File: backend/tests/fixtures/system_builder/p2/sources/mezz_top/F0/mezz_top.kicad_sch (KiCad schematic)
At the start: 2 parts, among them J1 DF12_Receptacle_2x10, J2 DF12_Receptacle_2x10

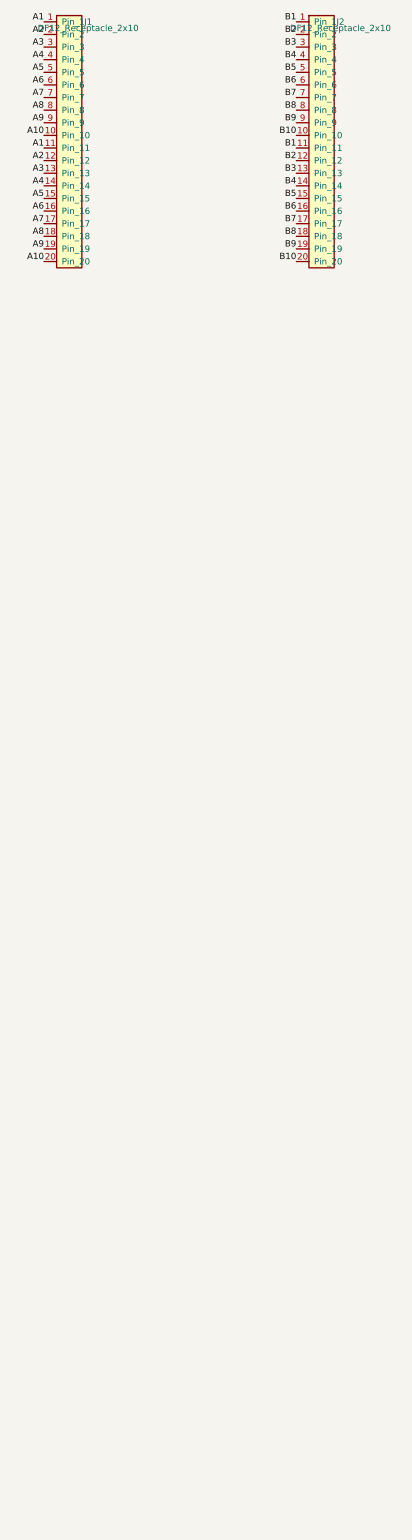
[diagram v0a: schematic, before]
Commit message: SB2-21: rebuild the mezzanine fixtures on Samtec ADM6/ADF6
The SB2-21 review moved the mezzanine pair from Hirose DF12(3.0) to Samtec
ADM6-30-03.5-L-4-0-A / ADF6-30-03.5-L-4-0-A, the JTYU OBC-to-CMBD pair.

- Footprints are written from Samtec's recommended PCB layouts (ADM6 rev G,
  ADF6 rev H): 4x30 at 0.635 mm, 0.356 mm pads, -A alignment NPTHs. They
  match Pixxel's ADM6-30 library footprint and CMBD's ADF6-30 pad for pad.
- Goldens: mated height 7.00 mm (ADX6 mated views, Table 1), top pose
  (0, 0, 8.6) mm, body heights G 4.900 / K 3.230 mm. The footprints name no
  orientation, so frames infer at medium confidence; goldens now pin the
  confidence of every frame.
- Samtec's STEP files (git-ignored, from the JTYU repos) are placed with
  rotate (-90 0 0); their alignment pins land on the NPTHs in KiCad's GLB
  export, which fixes the pin-1 end.
- All six boards clean on ERC, DRC with schematic parity, netlist, STEP and
  GLB with KiCad 10.0.6.
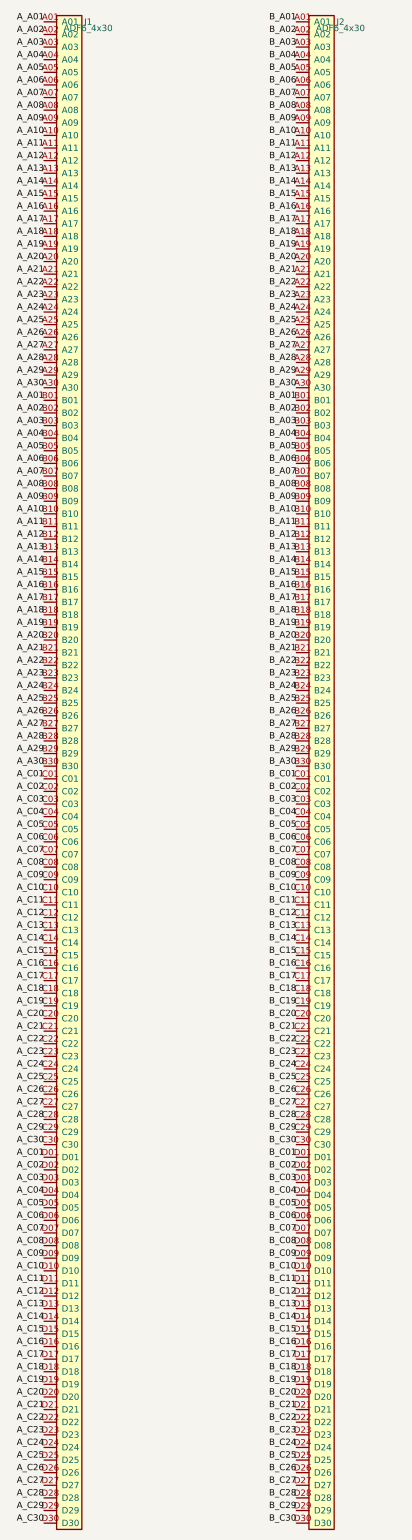
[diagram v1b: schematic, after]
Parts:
- J1, J2: value DF12_Receptacle_2x10 -> ADF6_4x30; footprint PrismFixture:Hirose_DF12_DF12C3.0-20DS-0.5V_2x10_P0.50mm_Vertical -> PrismFixture:Samtec_ADF6-30-03.5-L-4-0-A; symbol PrismFixture:DF12_Receptacle_2x10 -> PrismFixture:ADF6_4x30
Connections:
- removed net A1: J1.1 (Pin_1), J1.11 (Pin_11)
- removed net A10: J1.10 (Pin_10), J1.20 (Pin_20)
- removed net A2: J1.12 (Pin_12), J1.2 (Pin_2)
- removed net A3: J1.13 (Pin_13), J1.3 (Pin_3)
- removed net A4: J1.14 (Pin_14), J1.4 (Pin_4)
- removed net A5: J1.15 (Pin_15), J1.5 (Pin_5)
- removed net A6: J1.16 (Pin_16), J1.6 (Pin_6)
- removed net A7: J1.17 (Pin_17), J1.7 (Pin_7)
- removed net A8: J1.18 (Pin_18), J1.8 (Pin_8)
- removed net A9: J1.19 (Pin_19), J1.9 (Pin_9)
- removed net B1: J2.1 (Pin_1), J2.11 (Pin_11)
- removed net B10: J2.10 (Pin_10), J2.20 (Pin_20)
- removed net B2: J2.12 (Pin_12), J2.2 (Pin_2)
- removed net B3: J2.13 (Pin_13), J2.3 (Pin_3)
- removed net B4: J2.14 (Pin_14), J2.4 (Pin_4)
- removed net B5: J2.15 (Pin_15), J2.5 (Pin_5)
- removed net B6: J2.16 (Pin_16), J2.6 (Pin_6)
- removed net B7: J2.17 (Pin_17), J2.7 (Pin_7)
- removed net B8: J2.18 (Pin_18), J2.8 (Pin_8)
- removed net B9: J2.19 (Pin_19), J2.9 (Pin_9)
- new net A_A01: J1.A01, J1.B01
- new net A_A02: J1.A02, J1.B02
- new net A_A03: J1.A03, J1.B03
- new net A_A04: J1.A04, J1.B04
- new net A_A05: J1.A05, J1.B05
- new net A_A06: J1.A06, J1.B06
- new net A_A07: J1.A07, J1.B07
- new net A_A08: J1.A08, J1.B08
- new net A_A09: J1.A09, J1.B09
- new net A_A10: J1.A10, J1.B10
- new net A_A11: J1.A11, J1.B11
- new net A_A12: J1.A12, J1.B12
- new net A_A13: J1.A13, J1.B13
- new net A_A14: J1.A14, J1.B14
- new net A_A15: J1.A15, J1.B15
- new net A_A16: J1.A16, J1.B16
- new net A_A17: J1.A17, J1.B17
- new net A_A18: J1.A18, J1.B18
- new net A_A19: J1.A19, J1.B19
- new net A_A20: J1.A20, J1.B20
- new net A_A21: J1.A21, J1.B21
- new net A_A22: J1.A22, J1.B22
- new net A_A23: J1.A23, J1.B23
- new net A_A24: J1.A24, J1.B24
- new net A_A25: J1.A25, J1.B25
- new net A_A26: J1.A26, J1.B26
- new net A_A27: J1.A27, J1.B27
- new net A_A28: J1.A28, J1.B28
- new net A_A29: J1.A29, J1.B29
- new net A_A30: J1.A30, J1.B30
- new net A_C01: J1.C01, J1.D01
- new net A_C02: J1.C02, J1.D02
- new net A_C03: J1.C03, J1.D03
- new net A_C04: J1.C04, J1.D04
- new net A_C05: J1.C05, J1.D05
- new net A_C06: J1.C06, J1.D06
- new net A_C07: J1.C07, J1.D07
- new net A_C08: J1.C08, J1.D08
- new net A_C09: J1.C09, J1.D09
- new net A_C10: J1.C10, J1.D10
- new net A_C11: J1.C11, J1.D11
- new net A_C12: J1.C12, J1.D12
- new net A_C13: J1.C13, J1.D13
- new net A_C14: J1.C14, J1.D14
- new net A_C15: J1.C15, J1.D15
- new net A_C16: J1.C16, J1.D16
- new net A_C17: J1.C17, J1.D17
- new net A_C18: J1.C18, J1.D18
- new net A_C19: J1.C19, J1.D19
- new net A_C20: J1.C20, J1.D20
- new net A_C21: J1.C21, J1.D21
- new net A_C22: J1.C22, J1.D22
- new net A_C23: J1.C23, J1.D23
- new net A_C24: J1.C24, J1.D24
- new net A_C25: J1.C25, J1.D25
- new net A_C26: J1.C26, J1.D26
- new net A_C27: J1.C27, J1.D27
- new net A_C28: J1.C28, J1.D28
- new net A_C29: J1.C29, J1.D29
- new net A_C30: J1.C30, J1.D30
- new net B_A01: J2.A01, J2.B01
- new net B_A02: J2.A02, J2.B02
- new net B_A03: J2.A03, J2.B03
- new net B_A04: J2.A04, J2.B04
- new net B_A05: J2.A05, J2.B05
- new net B_A06: J2.A06, J2.B06
- new net B_A07: J2.A07, J2.B07
- new net B_A08: J2.A08, J2.B08
- new net B_A09: J2.A09, J2.B09
- new net B_A10: J2.A10, J2.B10
- new net B_A11: J2.A11, J2.B11
- new net B_A12: J2.A12, J2.B12
- new net B_A13: J2.A13, J2.B13
- new net B_A14: J2.A14, J2.B14
- new net B_A15: J2.A15, J2.B15
- new net B_A16: J2.A16, J2.B16
- new net B_A17: J2.A17, J2.B17
- new net B_A18: J2.A18, J2.B18
- new net B_A19: J2.A19, J2.B19
- new net B_A20: J2.A20, J2.B20
- new net B_A21: J2.A21, J2.B21
- new net B_A22: J2.A22, J2.B22
- new net B_A23: J2.A23, J2.B23
- new net B_A24: J2.A24, J2.B24
- new net B_A25: J2.A25, J2.B25
- new net B_A26: J2.A26, J2.B26
- new net B_A27: J2.A27, J2.B27
- new net B_A28: J2.A28, J2.B28
- new net B_A29: J2.A29, J2.B29
- new net B_A30: J2.A30, J2.B30
- new net B_C01: J2.C01, J2.D01
- new net B_C02: J2.C02, J2.D02
- new net B_C03: J2.C03, J2.D03
- new net B_C04: J2.C04, J2.D04
- new net B_C05: J2.C05, J2.D05
- new net B_C06: J2.C06, J2.D06
- new net B_C07: J2.C07, J2.D07
- new net B_C08: J2.C08, J2.D08
- new net B_C09: J2.C09, J2.D09
- new net B_C10: J2.C10, J2.D10
- new net B_C11: J2.C11, J2.D11
- new net B_C12: J2.C12, J2.D12
- new net B_C13: J2.C13, J2.D13
- new net B_C14: J2.C14, J2.D14
- new net B_C15: J2.C15, J2.D15
- new net B_C16: J2.C16, J2.D16
- new net B_C17: J2.C17, J2.D17
- new net B_C18: J2.C18, J2.D18
- new net B_C19: J2.C19, J2.D19
- new net B_C20: J2.C20, J2.D20
- new net B_C21: J2.C21, J2.D21
- new net B_C22: J2.C22, J2.D22
- new net B_C23: J2.C23, J2.D23
- new net B_C24: J2.C24, J2.D24
- new net B_C25: J2.C25, J2.D25
- new net B_C26: J2.C26, J2.D26
- new net B_C27: J2.C27, J2.D27
- new net B_C28: J2.C28, J2.D28
- new net B_C29: J2.C29, J2.D29
- new net B_C30: J2.C30, J2.D30
